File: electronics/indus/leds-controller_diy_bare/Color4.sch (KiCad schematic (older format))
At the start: 14 parts

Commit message: wip bare diy controller - dcdc and refactor
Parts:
- gave numbers to parts that had none: 14
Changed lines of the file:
@@
 $Descr A4 11693 8268
 encoding utf-8
-Sheet 6 8
+Sheet 6 9
 Title "Carte controlleur de LEDs 4 canaux"
 Date ""
@@
 VIN_24V
 $Comp
-L TPS92513 U?
+L TPS92513 U6
 U 1 1 57159E37
 P 5900 3600
-F 0 "U?" H 6250 2650 60  0000 C CNN
+F 0 "U6" H 6250 2650 60  0000 C CNN
 F 1 "TPS92513" H 5500 2650 60  0000 C CNN
 F 2 "" H 6050 3700 60  0000 C CNN
@@
 	1200 3500 5350 3500
 $Comp
-L GND-RESCUE-leds-controller #PWR?
+L GND-RESCUE-leds-controller #PWR022
 U 1 1 57159E3F
 P 3450 3150
-F 0 "#PWR?" H 3450 3150 30  0001 C CNN
+F 0 "#PWR022" H 3450 3150 30  0001 C CNN
 F 1 "GND" H 3450 3080 30  0001 C CNN
 F 2 "" H 3450 3150 60  0000 C CNN
@@
 $EndComp
 $Comp
-L C-RESCUE-leds-controller C?
+L C-RESCUE-leds-controller C25
 U 1 1 57159E45
 P 3450 2700
-F 0 "C?" H 3450 2800 40  0000 L CNN
+F 0 "C25" H 3450 2800 40  0000 L CNN
 F 1 "C" H 3456 2615 40  0000 L CNN
 F 2 "" H 3488 2550 30  0000 C CNN
@@
 $EndComp
 $Comp
-L R-RESCUE-leds-controller R?
+L R-RESCUE-leds-controller R29
 U 1 1 57159E4C
 P 4200 2750
-F 0 "R?" V 4280 2750 40  0000 C CNN
+F 0 "R29" V 4280 2750 40  0000 C CNN
 F 1 "R" V 4207 2751 40  0000 C CNN
 F 2 "" V 4130 2750 30  0000 C CNN
@@
 Connection ~ 4200 3500
 $Comp
-L C-RESCUE-leds-controller C?
+L C-RESCUE-leds-controller C23
 U 1 1 57159E56
 P 1700 4200
-F 0 "C?" H 1700 4300 40  0000 L CNN
+F 0 "C23" H 1700 4300 40  0000 L CNN
 F 1 "C" H 1706 4115 40  0000 L CNN
 F 2 "" H 1738 4050 30  0000 C CNN
@@
 Connection ~ 5850 4950
 $Comp
-L GND-RESCUE-leds-controller #PWR?
+L GND-RESCUE-leds-controller #PWR023
 U 1 1 57159E64
 P 6050 5300
-F 0 "#PWR?" H 6050 5300 30  0001 C CNN
+F 0 "#PWR023" H 6050 5300 30  0001 C CNN
 F 1 "GND" H 6050 5230 30  0001 C CNN
 F 2 "" H 6050 5300 60  0000 C CNN
@@
 Connection ~ 6050 4950
 $Comp
-L R-RESCUE-leds-controller R?
+L R-RESCUE-leds-controller R26
 U 1 1 57159E6B
 P 2250 3850
-F 0 "R?" V 2330 3850 40  0000 C CNN
+F 0 "R26" V 2330 3850 40  0000 C CNN
 F 1 "R" V 2257 3851 40  0000 C CNN
 F 2 "" V 2180 3850 30  0000 C CNN
@@
 $EndComp
 $Comp
-L R-RESCUE-leds-controller R?
+L R-RESCUE-leds-controller R27
 U 1 1 57159E72
 P 2250 4550
-F 0 "R?" V 2330 4550 40  0000 C CNN
+F 0 "R27" V 2330 4550 40  0000 C CNN
 F 1 "R" V 2257 4551 40  0000 C CNN
 F 2 "" V 2180 4550 30  0000 C CNN
@@
 Connection ~ 2250 4200
 $Comp
-L C-RESCUE-leds-controller C?
+L C-RESCUE-leds-controller C24
 U 1 1 57159E82
 P 3150 4350
-F 0 "C?" H 3150 4450 40  0000 L CNN
+F 0 "C24" H 3150 4450 40  0000 L CNN
 F 1 "C" H 3156 4265 40  0000 L CNN
 F 2 "" H 3188 4200 30  0000 C CNN
@@
 $EndComp
 $Comp
-L R-RESCUE-leds-controller R?
+L R-RESCUE-leds-controller R28
 U 1 1 57159E89
 P 4150 4550
-F 0 "R?" V 4230 4550 40  0000 C CNN
+F 0 "R28" V 4230 4550 40  0000 C CNN
 F 1 "R" V 4157 4551 40  0000 C CNN
 F 2 "" V 4080 4550 30  0000 C CNN
@@
 Connection ~ 4150 4950
 $Comp
-L INDUCTOR L?
+L INDUCTOR L5
 U 1 1 57159E98
 P 8300 3500
-F 0 "L?" V 8250 3500 40  0000 C CNN
+F 0 "L5" V 8250 3500 40  0000 C CNN
 F 1 "XAL6060-153MEC - 15µH - 6A" V 8400 3500 40  0000 C CNN
 F 2 "risebox:SELF_COILCRAFT_XAL6060-153" H 8300 3500 60  0001 C CNN
@@
 	6100 3000 6100 2300
 $Comp
-L C-RESCUE-leds-controller C?
+L C-RESCUE-leds-controller C26
 U 1 1 57159EA8
 P 6900 2950
-F 0 "C?" H 6900 3050 40  0000 L CNN
+F 0 "C26" H 6900 3050 40  0000 L CNN
 F 1 "C" H 6906 2865 40  0000 L CNN
 F 2 "" H 6938 2800 30  0000 C CNN
@@
 	8600 3500 10550 3500
 $Comp
-L C-RESCUE-leds-controller C?
+L C-RESCUE-leds-controller C27
 U 1 1 57159EB9
 P 9650 3800
-F 0 "C?" H 9650 3900 40  0000 L CNN
+F 0 "C27" H 9650 3900 40  0000 L CNN
 F 1 "C" H 9656 3715 40  0000 L CNN
 F 2 "" H 9688 3650 30  0000 C CNN
@@
 Connection ~ 9650 4100
 $Comp
-L R-RESCUE-leds-controller R?
+L R-RESCUE-leds-controller R30
 U 1 1 57159EC4
 P 8300 4100
-F 0 "R?" V 8380 4100 40  0000 C CNN
+F 0 "R30" V 8380 4100 40  0000 C CNN
 F 1 "R" V 8307 4101 40  0000 C CNN
 F 2 "" V 8230 4100 30  0000 C CNN
@@
 	8550 4100 10550 4100
 $Comp
-L R-RESCUE-leds-controller R?
+L R-RESCUE-leds-controller R31
 U 1 1 57159ECD
 P 10250 4550
-F 0 "R?" V 10330 4550 40  0000 C CNN
+F 0 "R31" V 10330 4550 40  0000 C CNN
 F 1 "R" V 10257 4551 40  0000 C CNN
 F 2 "" V 10180 4550 30  0000 C CNN
@@
 	10250 4950 10250 4800
 $Comp
-L DIODESCH D?
+L DIODESCH D6
 U 1 1 57159ED7
 P 7450 4550
-F 0 "D?" H 7450 4650 40  0000 C CNN
+F 0 "D6" H 7450 4650 40  0000 C CNN
 F 1 "DIODESCH" H 7450 4450 40  0000 C CNN
 F 2 "" H 7450 4550 60  0000 C CNN

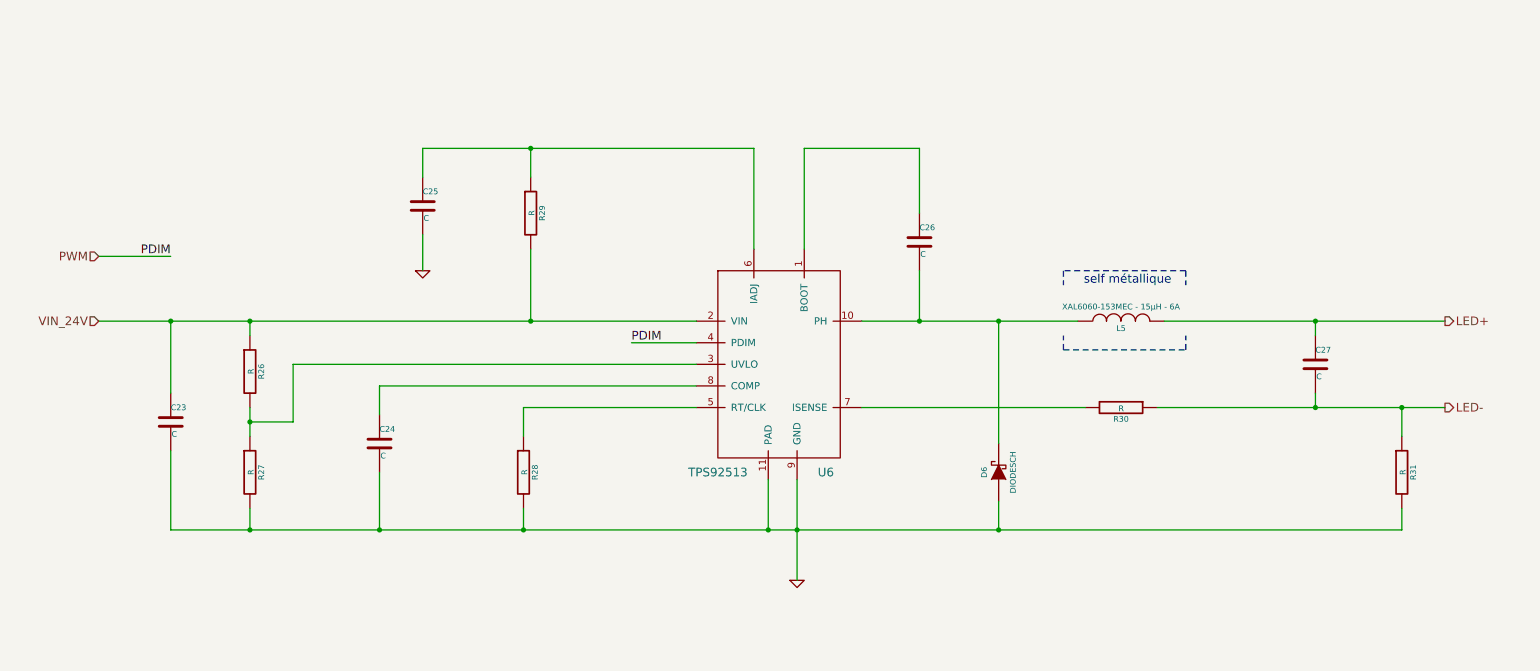
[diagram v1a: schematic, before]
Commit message: schema done - misses values
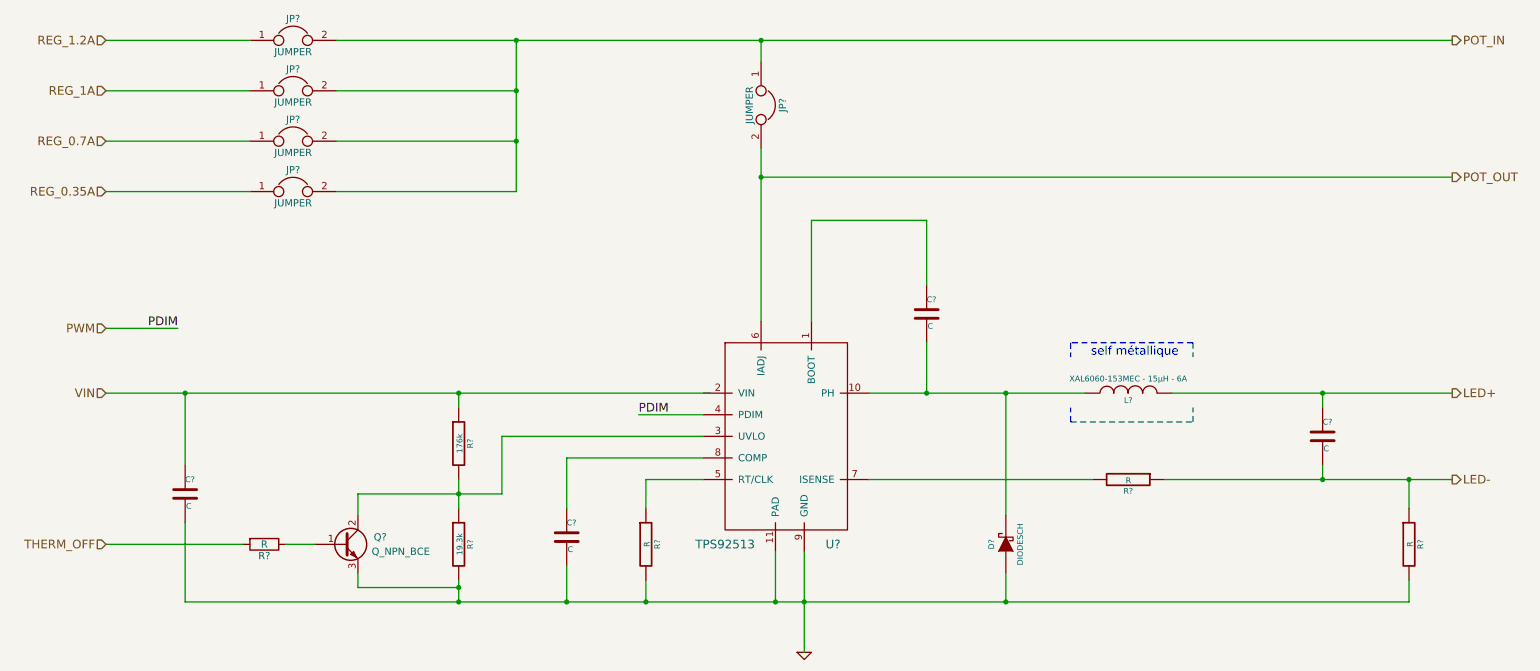
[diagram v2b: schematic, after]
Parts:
- removed C23, C24, C25, C26, C27: C, symbol C-RESCUE-leds-controller
- removed D6: DIODESCH, symbol DIODESCH
- removed L5: XAL6060-153MEC - 15µH - 6A, risebox:SELF_COILCRAFT_XAL6060-153, symbol INDUCTOR
- removed R26, R27, R28, R29, R30, R31: R, symbol R-RESCUE-leds-controller
- removed U6: TPS92513, symbol TPS92513
- added C? (x4): C, symbol C-RESCUE-leds-controller
- added D?: DIODESCH, symbol DIODESCH
- added JP? (x5): JUMPER, symbol JUMPER
- added L?: XAL6060-153MEC - 15µH - 6A, risebox:SELF_COILCRAFT_XAL6060-153, symbol INDUCTOR
- added Q?: Q_NPN_BCE, symbol Q_NPN_BCE
- added R?: 176k, symbol R-RESCUE-leds-controller
- added R?: 19.3k, symbol R-RESCUE-leds-controller
- added R? (x3): R, symbol R-RESCUE-leds-controller
- added R?: R, symbol R
- added U?: TPS92513, symbol TPS92513
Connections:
- net GND: now also C?.2, C?.2, D?.1 (A), Q?.3 (E), R?.2, R?.2, R?.2, U?.11 (PAD), U?.9 (GND)
- net LED+: now also C?.1, L?.2
- net LED-: now also C?.2, R?.1, R?.1
- net PWM: now also U?.4 (PDIM)
- new net: C?.1, U?.1 (BOOT)
- new net: C?.2, D?.2 (K), L?.1, U?.10 (PH)
- new net: Q?.2 (C), R?.1, R?.2, U?.3 (UVLO)
- new net: R?.1, U?.5 (RT/CLK)
- new net: R?.2, U?.7 (ISENSE)
- new net: C?.1, U?.8 (COMP)
- new net: Q?.1 (B), R?.1
- new net POT_IN: JP?.1, JP?.2, JP?.2, JP?.2, JP?.2
- new net POT_OUT: JP?.2, U?.6 (IADJ)
- new net REG_0.35A: JP?.1
- new net REG_0.7A: JP?.1
- new net REG_1.2A: JP?.1
- new net REG_1A: JP?.1
- new net THERM_OFF: R?.2
- new net VIN: C?.1, R?.1

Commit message: schema prctically ok missing refs
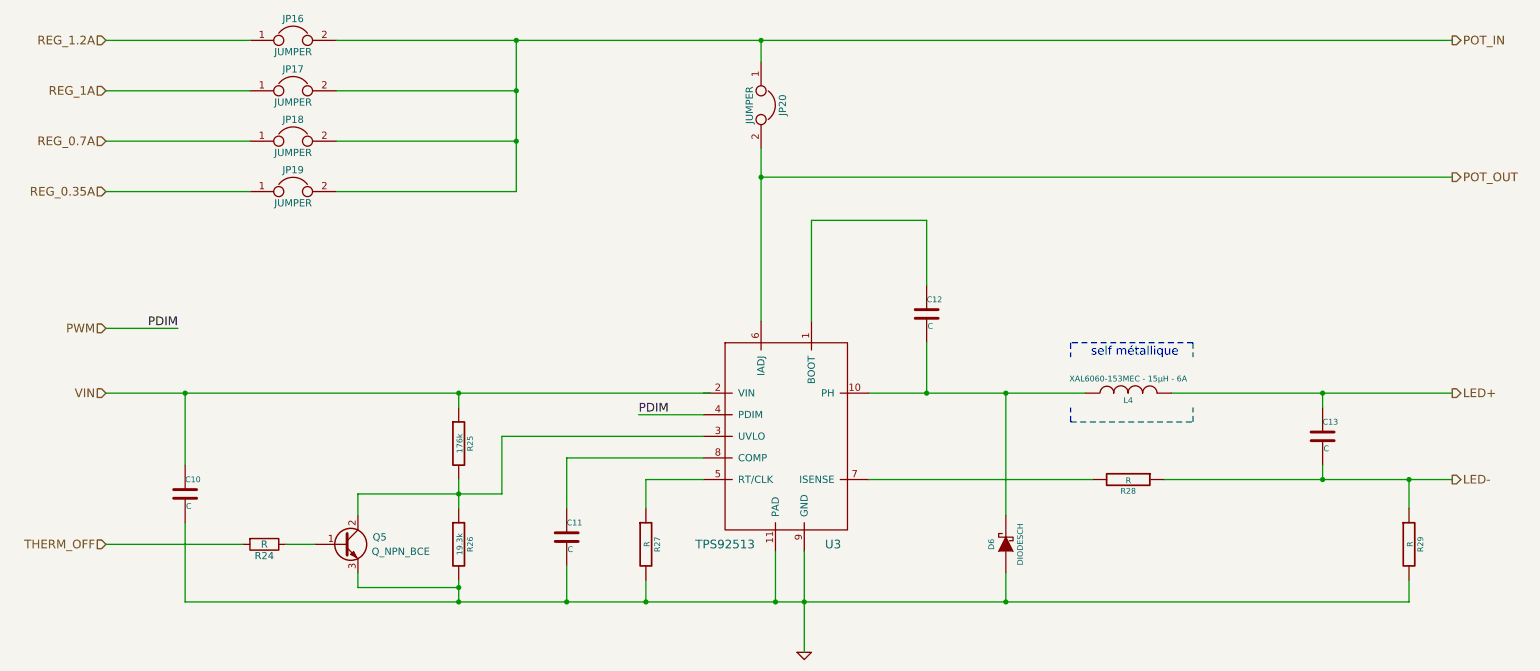
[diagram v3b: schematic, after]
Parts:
- gave numbers to parts that had none: 19
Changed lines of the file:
@@
 VIN
 $Comp
-L TPS92513 U?
+L TPS92513 U3
 U 1 1 57672FFD
 P 5950 4100
-F 0 "U?" H 6300 3150 60  0000 C CNN
+F 0 "U3" H 6300 3150 60  0000 C CNN
 F 1 "TPS92513" H 5550 3150 60  0000 C CNN
 F 2 "" H 6100 4200 60  0000 C CNN
@@
 $EndComp
 $Comp
-L C-RESCUE-leds-controller C?
+L C-RESCUE-leds-controller C10
 U 1 1 57673004
 P 1800 4700
-F 0 "C?" H 1800 4800 40  0000 L CNN
+F 0 "C10" H 1800 4800 40  0000 L CNN
 F 1 "C" H 1806 4615 40  0000 L CNN
 F 2 "" H 1838 4550 30  0000 C CNN
@@
 $EndComp
 $Comp
-L GND-RESCUE-leds-controller #PWR?
+L GND-RESCUE-leds-controller #PWR14
 U 1 1 5767300B
 P 6100 5800
-F 0 "#PWR?" H 6100 5800 30  0001 C CNN
+F 0 "#PWR14" H 6100 5800 30  0001 C CNN
 F 1 "GND" H 6100 5730 30  0001 C CNN
 F 2 "" H 6100 5800 60  0000 C CNN
@@
 $EndComp
 $Comp
-L R-RESCUE-leds-controller R?
+L R-RESCUE-leds-controller R25
 U 1 1 57673011
 P 3700 4350
-F 0 "R?" V 3780 4350 40  0000 C CNN
+F 0 "R25" V 3780 4350 40  0000 C CNN
 F 1 "176k" V 3707 4351 40  0000 C CNN
 F 2 "" V 3630 4350 30  0000 C CNN
@@
 $EndComp
 $Comp
-L R-RESCUE-leds-controller R?
+L R-RESCUE-leds-controller R26
 U 1 1 57673018
 P 3700 5050
-F 0 "R?" V 3780 5050 40  0000 C CNN
+F 0 "R26" V 3780 5050 40  0000 C CNN
 F 1 "19.3k" V 3707 5051 40  0000 C CNN
 F 2 "" V 3630 5050 30  0000 C CNN
@@
 $EndComp
 $Comp
-L C-RESCUE-leds-controller C?
+L C-RESCUE-leds-controller C11
 U 1 1 5767301F
 P 4450 5000
-F 0 "C?" H 4450 5100 40  0000 L CNN
+F 0 "C11" H 4450 5100 40  0000 L CNN
 F 1 "C" H 4456 4915 40  0000 L CNN
 F 2 "" H 4488 4850 30  0000 C CNN
@@
 $EndComp
 $Comp
-L R-RESCUE-leds-controller R?
+L R-RESCUE-leds-controller R27
 U 1 1 57673026
 P 5000 5050
-F 0 "R?" V 5080 5050 40  0000 C CNN
+F 0 "R27" V 5080 5050 40  0000 C CNN
 F 1 "R" V 5007 5051 40  0000 C CNN
 F 2 "" V 4930 5050 30  0000 C CNN
@@
 $EndComp
 $Comp
-L INDUCTOR L?
+L INDUCTOR L4
 U 1 1 5767302D
 P 8350 4000
-F 0 "L?" V 8300 4000 40  0000 C CNN
+F 0 "L4" V 8300 4000 40  0000 C CNN
 F 1 "XAL6060-153MEC - 15µH - 6A" V 8450 4000 40  0000 C CNN
 F 2 "risebox:SELF_COILCRAFT_XAL6060-153" H 8350 4000 60  0001 C CNN
@@
 self métallique
 $Comp
-L C-RESCUE-leds-controller C?
+L C-RESCUE-leds-controller C12
 U 1 1 57673035
 P 6950 3450
-F 0 "C?" H 6950 3550 40  0000 L CNN
+F 0 "C12" H 6950 3550 40  0000 L CNN
 F 1 "C" H 6956 3365 40  0000 L CNN
 F 2 "" H 6988 3300 30  0000 C CNN
@@
 $EndComp
 $Comp
-L C-RESCUE-leds-controller C?
+L C-RESCUE-leds-controller C13
 U 1 1 5767303C
 P 9700 4300
-F 0 "C?" H 9700 4400 40  0000 L CNN
+F 0 "C13" H 9700 4400 40  0000 L CNN
 F 1 "C" H 9706 4215 40  0000 L CNN
 F 2 "" H 9738 4150 30  0000 C CNN
@@
 $EndComp
 $Comp
-L R-RESCUE-leds-controller R?
+L R-RESCUE-leds-controller R28
 U 1 1 57673043
 P 8350 4600
-F 0 "R?" V 8430 4600 40  0000 C CNN
+F 0 "R28" V 8430 4600 40  0000 C CNN
 F 1 "R" V 8357 4601 40  0000 C CNN
 F 2 "" V 8280 4600 30  0000 C CNN
@@
 $EndComp
 $Comp
-L R-RESCUE-leds-controller R?
+L R-RESCUE-leds-controller R29
 U 1 1 5767304A
 P 10300 5050
-F 0 "R?" V 10380 5050 40  0000 C CNN
+F 0 "R29" V 10380 5050 40  0000 C CNN
 F 1 "R" V 10307 5051 40  0000 C CNN
 F 2 "" V 10230 5050 30  0000 C CNN
@@
 $EndComp
 $Comp
-L DIODESCH D?
+L DIODESCH D6
 U 1 1 57673051
 P 7500 5050
-F 0 "D?" H 7500 5150 40  0000 C CNN
+F 0 "D6" H 7500 5150 40  0000 C CNN
 F 1 "DIODESCH" H 7500 4950 40  0000 C CNN
 F 2 "" H 7500 5050 60  0000 C CNN
@@
 PDIM
 $Comp
-L JUMPER JP?
+L JUMPER JP16
 U 1 1 5767305B
 P 2550 1550
-F 0 "JP?" H 2550 1700 50  0000 C CNN
+F 0 "JP16" H 2550 1700 50  0000 C CNN
 F 1 "JUMPER" H 2550 1470 50  0000 C CNN
 F 2 "" H 2550 1550 50  0000 C CNN
@@
 $EndComp
 $Comp
-L JUMPER JP?
+L JUMPER JP17
 U 1 1 57673062
 P 2550 1900
-F 0 "JP?" H 2550 2050 50  0000 C CNN
+F 0 "JP17" H 2550 2050 50  0000 C CNN
 F 1 "JUMPER" H 2550 1820 50  0000 C CNN
 F 2 "" H 2550 1900 50  0000 C CNN
@@
 $EndComp
 $Comp
-L JUMPER JP?
+L JUMPER JP18
 U 1 1 57673069
 P 2550 2250
-F 0 "JP?" H 2550 2400 50  0000 C CNN
+F 0 "JP18" H 2550 2400 50  0000 C CNN
 F 1 "JUMPER" H 2550 2170 50  0000 C CNN
 F 2 "" H 2550 2250 50  0000 C CNN
@@
 $EndComp
 $Comp
-L JUMPER JP?
+L JUMPER JP19
 U 1 1 57673070
 P 2550 2600
-F 0 "JP?" H 2550 2750 50  0000 C CNN
+F 0 "JP19" H 2550 2750 50  0000 C CNN
 F 1 "JUMPER" H 2550 2520 50  0000 C CNN
 F 2 "" H 2550 2600 50  0000 C CNN
@@
 REG_0.35A
 $Comp
-L JUMPER JP?
+L JUMPER JP20
 U 1 1 5767307B
 P 5800 2000
-F 0 "JP?" H 5800 2150 50  0000 C CNN
+F 0 "JP20" H 5800 2150 50  0000 C CNN
 F 1 "JUMPER" H 5800 1920 50  0000 C CNN
 F 2 "" H 5800 2000 50  0000 C CNN
@@
 Connection ~ 3700 5350
 $Comp
-L Q_NPN_BCE Q?
+L Q_NPN_BCE Q5
 U 1 1 576730E6
 P 2900 5050
-F 0 "Q?" H 3200 5100 50  0000 R CNN
+F 0 "Q5" H 3200 5100 50  0000 R CNN
 F 1 "Q_NPN_BCE" H 3500 5000 50  0000 R CNN
 F 2 "" H 3100 5150 50  0000 C CNN
@@
 THERM_OFF
 $Comp
-L R R?
+L R R24
 U 1 1 576730EE
 P 2350 5050
-F 0 "R?" V 2430 5050 50  0000 C CNN
+F 0 "R24" V 2430 5050 50  0000 C CNN
 F 1 "R" V 2350 5050 50  0000 C CNN
 F 2 "" V 2280 5050 50  0000 C CNN
